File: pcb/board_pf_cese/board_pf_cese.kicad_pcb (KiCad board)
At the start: 2 copper layers, 120 x 100 mm, 17 parts, among them J1 Screw_Terminal_01x02, J2 Conn_01x04, J3 Conn_01x04, J4 Conn_01x04, J5 Conn_01x04, J6 Conn_01x15, J7 Conn_01x15, J8 Conn_01x08, J9 Conn_01x08

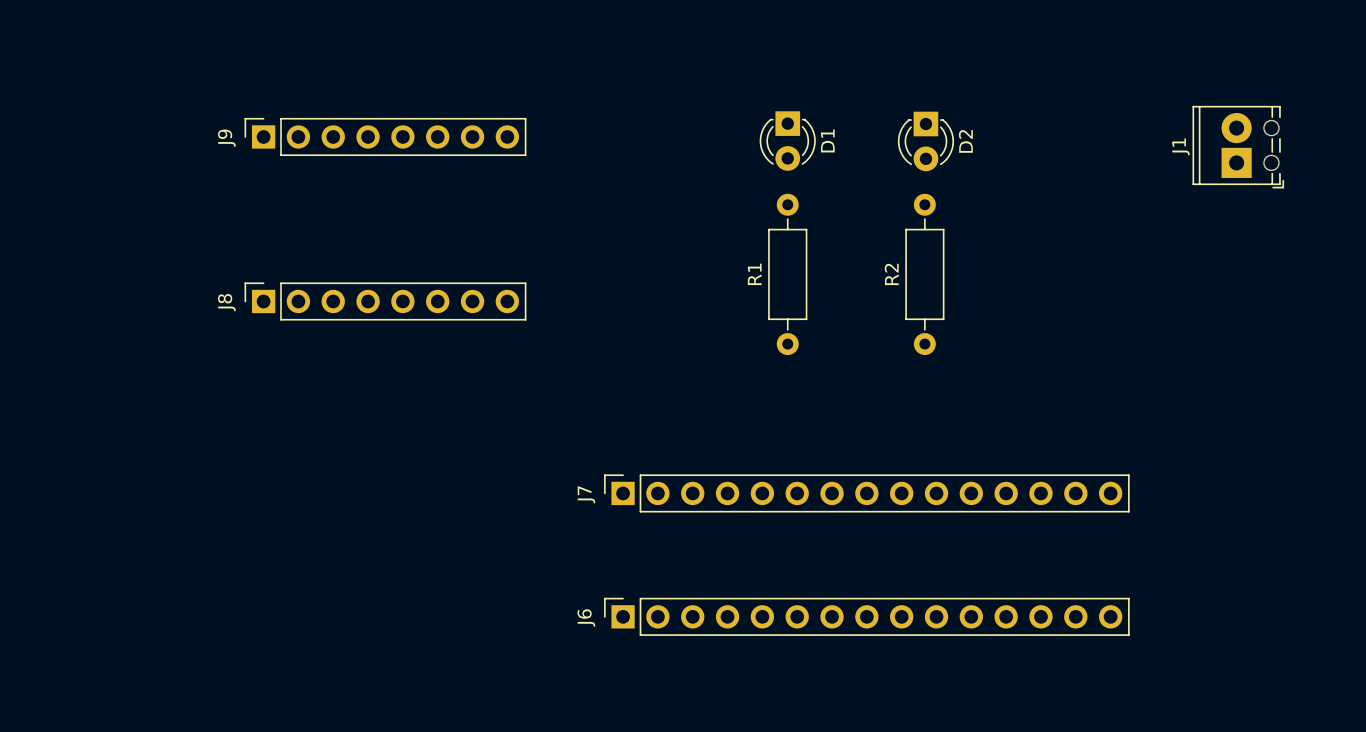
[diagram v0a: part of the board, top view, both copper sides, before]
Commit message: se agrego el archvo git ignore
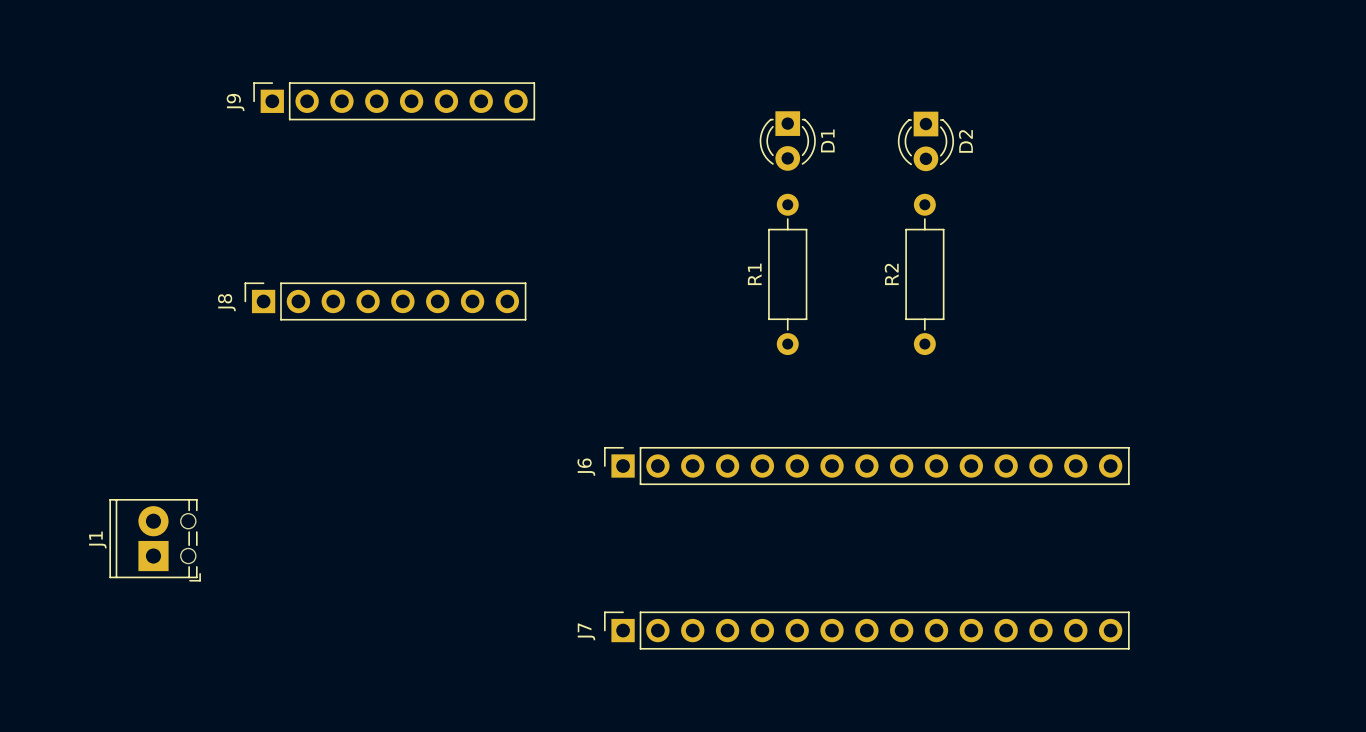
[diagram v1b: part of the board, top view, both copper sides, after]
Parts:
- moved J1 84.0 mm to (112.0, 107.5)
- moved J6 11.0 mm to (146.2, 101.0)
- moved J7 10.0 mm to (146.2, 113.0)
- moved J9 2.68 mm to (120.7, 74.4)
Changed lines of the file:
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@@
   )
   (footprint "TerminalBlock_Phoenix:TerminalBlock_Phoenix_MPT-0,5-2-2.54_1x02_P2.54mm_Horizontal" (layer "F.Cu")
-    (at 191 78.866 90)
+    (at 112 107.54 90)
     (descr "Terminal Block Phoenix MPT-0,5-2-2.54, 2 pins, pitch 2.54mm, size 5.54x6.2mm^2, drill diamater 1.1mm, pad diameter 2.2mm, see http://www.mouser.com/ds/2/324/ItemDetail_1725656-920552.pdf, script-generated using https://github.com/pointhi/kicad-footprint-generator/scripts/TerminalBlock_Phoenix")
     (tags "THT Terminal Block Phoenix MPT-0,5-2-2.54 pitch 2.54mm size 5.54x6.2mm^2 drill 1.1mm pad 2.2mm")
@@
   )
   (footprint "Connector_PinSocket_2.54mm:PinSocket_1x15_P2.54mm_Vertical" (layer "F.Cu")
-    (at 146.25 102.975 90)
+    (at 146.25 112.975 90)
     (descr "Through hole straight socket strip, 1x15, 2.54mm pitch, single row (from Kicad 4.0.7), script generated")
     (tags "Through hole socket strip THT 1x15 2.54mm single row")
@@
   )
   (footprint "Connector_PinSocket_2.54mm:PinSocket_1x08_P2.54mm_Vertical" (layer "F.Cu")
-    (at 120.03 76.975 90)
+    (at 120.665 74.375 90)
     (descr "Through hole straight socket strip, 1x08, 2.54mm pitch, single row (from Kicad 4.0.7), script generated")
     (tags "Through hole socket strip THT 1x08 2.54mm single row")
@@
   )
   (footprint "Connector_PinSocket_2.54mm:PinSocket_1x15_P2.54mm_Vertical" (layer "F.Cu")
-    (at 146.25 111.975 90)
+    (at 146.25 100.975 90)
     (descr "Through hole straight socket strip, 1x15, 2.54mm pitch, single row (from Kicad 4.0.7), script generated")
     (tags "Through hole socket strip THT 1x15 2.54mm single row")

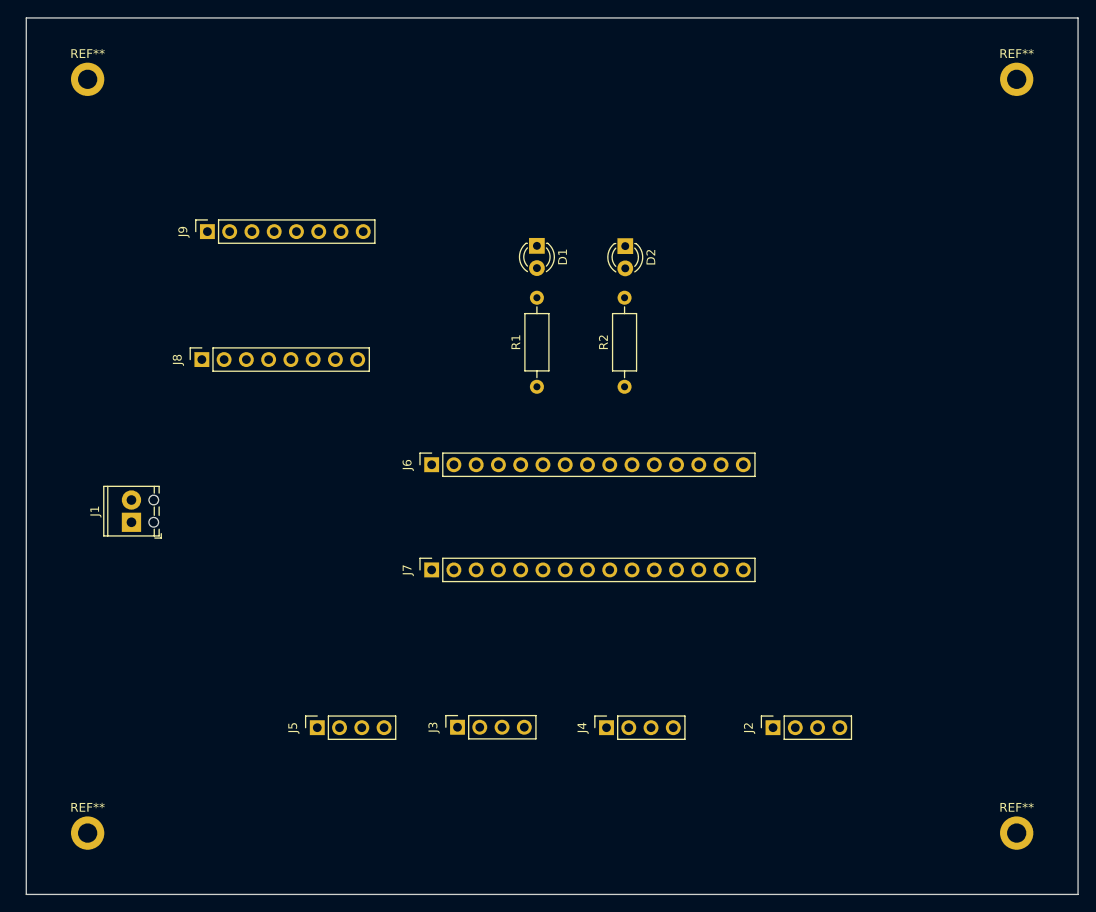
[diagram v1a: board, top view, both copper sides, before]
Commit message: se redimensiono el tamaño del pcb
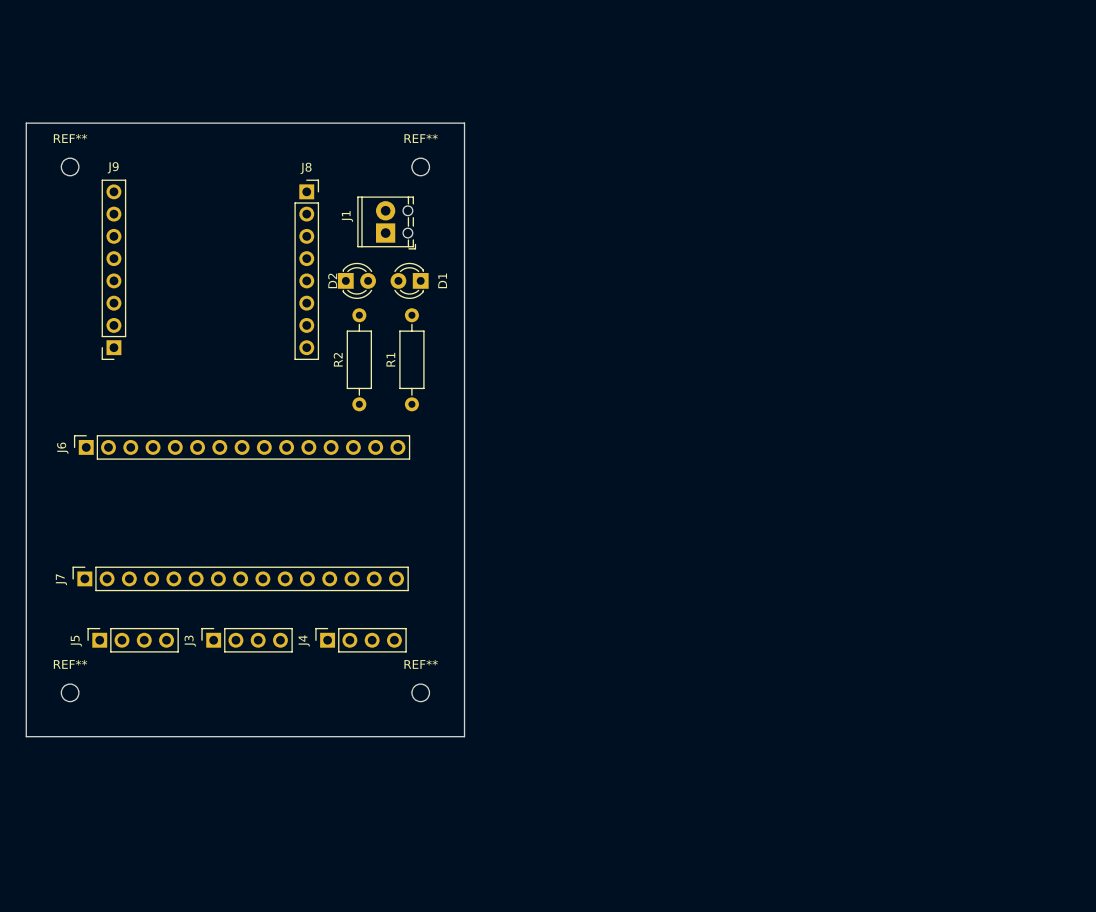
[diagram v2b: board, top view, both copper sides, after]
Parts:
- removed J2: Conn_01x04, Connector_PinSocket_2.54mm:PinSocket_1x04_P2.54mm_Vertical
- removed the REF** at (213.0, 143.0)
- removed the REF** at (107.0, 57.0)
- removed the REF** at (213.0, 57.0)
- removed the REF** at (107.0, 143.0)
- added REF**: MountingHole_2mm, MountingHole:MountingHole_2mm, F.Cu at (105.0, 127.0)
- added REF**: MountingHole_2mm, MountingHole:MountingHole_2mm, F.Cu at (105.0, 67.0)
- added REF**: MountingHole_2mm, MountingHole:MountingHole_2mm, F.Cu at (145.0, 127.0)
- added REF**: MountingHole_2mm, MountingHole:MountingHole_2mm, F.Cu at (145.0, 67.0)
- moved J1 43.9 mm to (141.0, 74.5)
- moved J7 39.6 mm to (106.7, 114.0)
- moved J6 39.5 mm to (106.8, 99.0)
- moved J4 33.3 mm to (134.4, 121.0)
- moved D2 32.1 mm to (136.5, 80.0), turned to 0 degrees
- moved R2 30.3 mm to (138.0, 94.1)
- moved J3 29.5 mm to (121.4, 121.0)
- moved J5 26.7 mm to (108.4, 121.0)
- moved J8 22.6 mm to (132.0, 69.8), turned to 0 degrees
- moved J9 17.0 mm to (110.0, 87.6), turned to 180 degrees
- moved R1 14.4 mm to (144.0, 94.1)
- moved D1 13.9 mm to (145.0, 80.0), turned to 180 degrees
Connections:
- J6 pad 6: Net-(J2-Pad4) -> unconnected-(J6-Pin_6-Pad6)
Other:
- board size 120 x 100 mm -> 50 x 70 mm

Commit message: ruteo con errores
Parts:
- added J2: Conn_01x04, Connector_PinSocket_2.54mm:PinSocket_1x04_P2.54mm_Vertical, F.Cu at (114.0, 122.0)
- moved J6 39.6 mm to (142.6, 116.0), turned to -90 degrees
- moved J7 38.2 mm to (142.6, 100.8), turned to -90 degrees
- moved J9 27.5 mm to (131.9, 71.0), turned to 0 degrees
- moved J8 23.0 mm to (109.0, 71.0)
- moved J5 21.5 mm to (129.0, 127.0)
- moved J4 21.2 mm to (114.0, 127.0)
- moved J3 7.61 mm to (128.9, 122.0)
- moved J1 3.00 mm to (144.0, 74.5)
- moved D2 2.73 mm to (139.0, 79.0), turned to -90 degrees
- moved R1 1.41 mm to (145.0, 95.1)
- moved R2 1.41 mm to (139.0, 95.1)
- moved D1 1.00 mm to (145.0, 79.0), turned to -90 degrees
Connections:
- J6 pad 10: unconnected-(J6-Pin_10-Pad10) -> Net-(J4-Pin_3)
- J6 pad 3: /N_RST -> unconnected-(J6-Pin_3-Pad3)
- J6 pad 4: +5V -> unconnected-(J6-Pin_4-Pad4)
- J6 pad 6: unconnected-(J6-Pin_6-Pad6) -> /SCL
- J6 pad 7: Net-(J3-Pin_4) -> unconnected-(J6-Pin_7-Pad7)
- J6 pad 8: Net-(J4-Pin_3) -> Net-(J3-Pin_4)
- J6 pad 9: unconnected-(J6-Pin_9-Pad9) -> Net-(J2-Pin_4)
- J7 pad 1: /SCL -> /M_TX
- J7 pad 10: Net-(J7-Pin_10) -> unconnected-(J7-Pin_10-Pad10)
- J7 pad 13: unconnected-(J7-Pin_13-Pad13) -> /SE
- J7 pad 15: unconnected-(J7-Pin_15-Pad15) -> /SDA
- J7 pad 2: /SDA -> /M_RX
- J7 pad 3: /N_RST -> unconnected-(J7-Pin_3-Pad3)
- J7 pad 5: unconnected-(J7-Pin_5-Pad5) -> /OR
- J7 pad 6: unconnected-(J7-Pin_6-Pad6) -> /SO
- J7 pad 7: /M_TX -> unconnected-(J7-Pin_7-Pad7)
- J7 pad 8: /M_RX -> unconnected-(J7-Pin_8-Pad8)
- J7 pad 9: /PU -> unconnected-(J7-Pin_9-Pad9)
- J8 pad 2: /PU -> /OR
- J9 pad 7: +5V -> unconnected-(J9-Pin_7-Pad7)
- R1 pad 1: Net-(J7-Pin_10) -> /SO
- R2 pad 1: +3.3V -> /SE
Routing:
- net /SDA: track 0.00 -> 67.8 mm
- net /OR: track 0.00 -> 47.6 mm
- net /SCL: track 0.00 -> 41.3 mm
- net /M_TX: track 0.00 -> 33.9 mm
- net /M_RX: track 0.00 -> 33.5 mm
- net /SE: track 0.00 -> 30.0 mm
- net Net-(J4-Pin_3): track 0.00 -> 27.8 mm
- net /SO: track 0.00 -> 19.3 mm
- net Net-(J3-Pin_4): track 0.00 -> 16.0 mm
- net Net-(J2-Pin_4): track 0.00 -> 6.26 mm
- net Net-(D2-A): track 0.00 -> 3.38 mm
- net Net-(D1-A): track 0.00 -> 3.38 mm
- added copper zone on F.Cu, net +3.3V
- added copper zone on B.Cu, net GND

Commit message: ruteo terminado
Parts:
- added REF**: KiCad-Logo2_5mm_SilkScreen, Symbol:KiCad-Logo2_5mm_SilkScreen, B.Cu at (124.0, 107.0)
- renumbered REF** to REF1, REF** to REF2, REF** to REF3, REF** to REF4
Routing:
- net GND: track 0.00 -> 8.71 mm, vias 0 -> 1
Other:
- board text added: "Ing. Mario Aguilar"

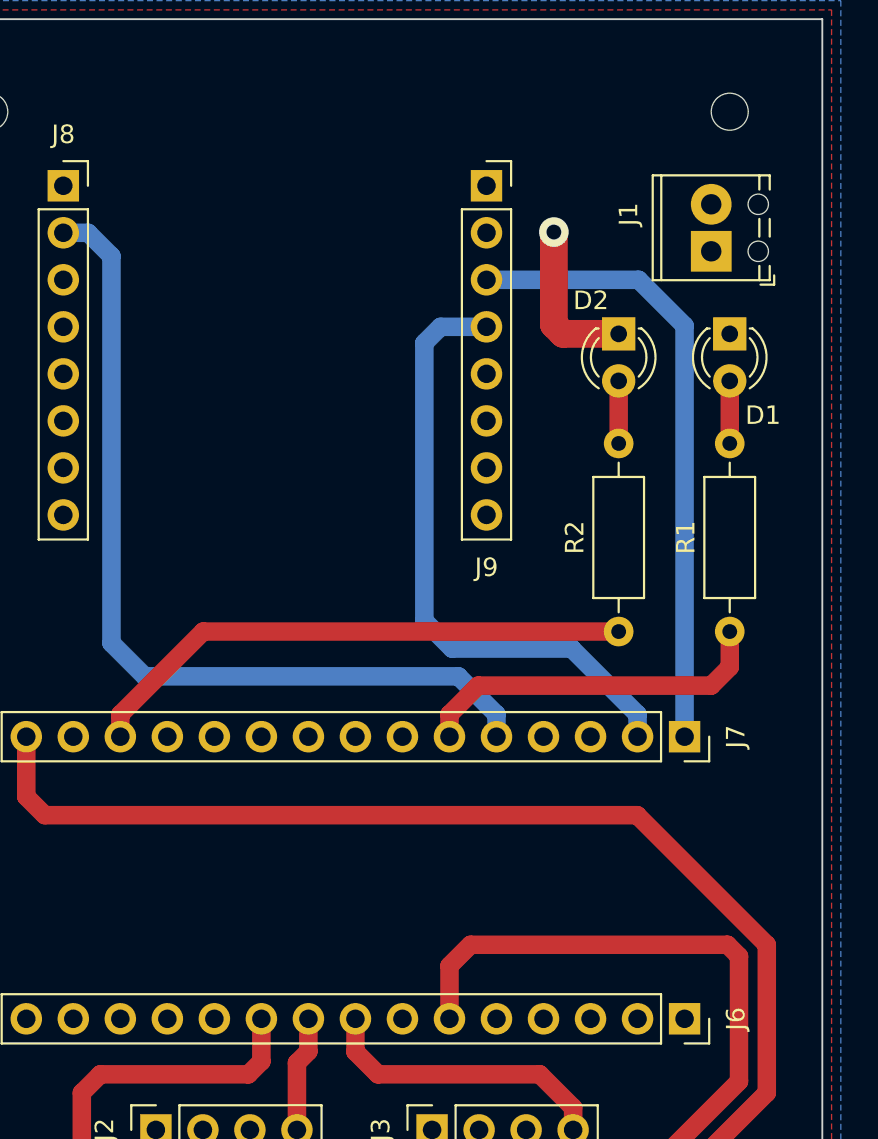
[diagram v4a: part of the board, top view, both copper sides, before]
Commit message: se actualizo el metodo de alimentacion
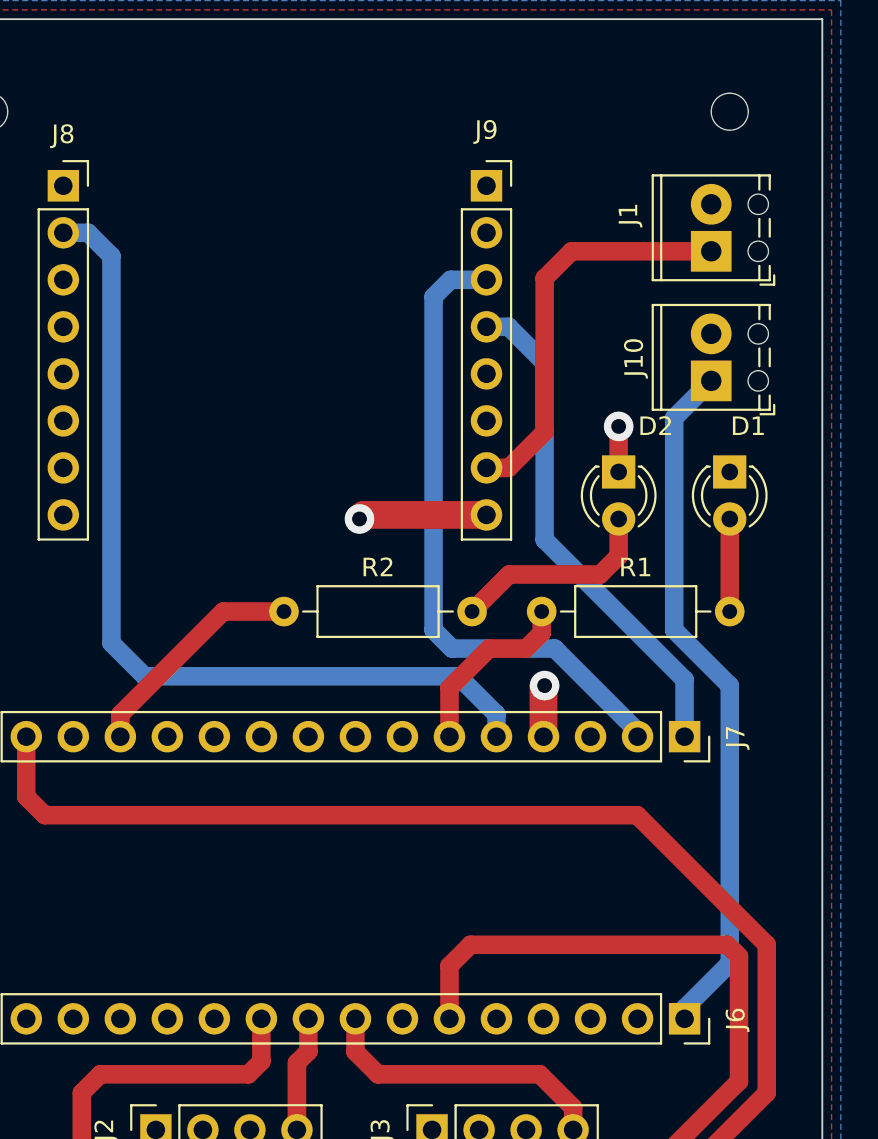
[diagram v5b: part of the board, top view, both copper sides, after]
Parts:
- added J10: Screw_Terminal_01x02, TerminalBlock_Phoenix:TerminalBlock_Phoenix_MPT-0,5-2-2.54_1x02_P2.54mm_Horizontal, F.Cu at (144.0, 81.5)
- moved R2 18.1 mm to (120.9, 94.0), turned to 0 degrees
- moved R1 10.2 mm to (134.8, 94.0), turned to 0 degrees
- moved D1 7.46 mm to (145.0, 86.5)
- moved D2 7.46 mm to (139.0, 86.5)
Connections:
- J1 pad 1: +3.3V -> +5V
- J6 pad 1: unconnected-(J6-Pin_1-Pad1) -> +12V
- J7 pad 1: /M_TX -> /M_RX
- J7 pad 2: /M_RX -> /M_TX
- J9 pad 7: unconnected-(J9-Pin_7-Pad7) -> +5V
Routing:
- net +12V: track 0.00 -> 37.5 mm
- net +5V: track 0.00 -> 21.8 mm
- net /SE: track 30.0 -> 12.3 mm
- net /SO: track 19.3 -> 9.99 mm
- net Net-(D2-A): track 3.38 -> 11.2 mm
- net /M_RX: track 33.5 -> 27.3 mm
- net GND: track 8.71 -> 12.2 mm, vias 1 -> 3
- net Net-(D1-A): track 3.38 -> 5.00 mm
- net /M_TX: track 33.9 -> 34.8 mm

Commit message: se adiciono conn uart2 para debug
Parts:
- added J11: Conn_01x05, Connector_PinSocket_2.54mm:PinSocket_1x05_P2.54mm_Vertical, F.Cu at (106.9, 96.0)
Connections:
- J6 pad 5: unconnected-(J6-Pin_5-Pad5) -> /UART2_TX
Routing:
- net /UART2_TX: track 0.00 -> 67.3 mm, vias 0 -> 1
- net /OR: track 47.6 -> 43.5 mm
- net /SCL: track 41.3 -> 42.9 mm
- net /SE: track 12.3 -> 13.6 mm

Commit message: corrigio posicionamiento del conn debug
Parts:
- moved J11 1.00 mm to (106.9, 95.0)
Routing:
- net /UART2_TX: track 67.3 -> 68.3 mm
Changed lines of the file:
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@@
   )
   (footprint "Connector_PinSocket_2.54mm:PinSocket_1x05_P2.54mm_Vertical" (layer "F.Cu")
-    (at 106.92 96 90)
+    (at 106.92 95 90)
     (descr "Through hole straight socket strip, 1x05, 2.54mm pitch, single row (from Kicad 4.0.7), script generated")
     (tags "Through hole socket strip THT 1x05 2.54mm single row")
@@
   (segment (start 107 107) (end 104 104) (width 1) (layer "F.Cu") (net 12))
   (segment (start 140 108) (end 139 107) (width 1) (layer "F.Cu") (net 12))
+  (segment (start 112 97.202081) (end 112 95) (width 1) (layer "F.Cu") (net 12))
   (segment (start 139 107) (end 107 107) (width 1) (layer "F.Cu") (net 12))
   (segment (start 111.202081 98) (end 112 97.202081) (width 1) (layer "F.Cu") (net 12))
@@
   (segment (start 105 98) (end 111.202081 98) (width 1) (layer "F.Cu") (net 12))
   (segment (start 104 104) (end 104 99) (width 1) (layer "F.Cu") (net 12))
-  (segment (start 112 97.202081) (end 112 96) (width 1) (layer "F.Cu") (net 12))
   (via (at 140 108) (size 1.6) (drill 0.8) (layers "F.Cu" "B.Cu") (net 12))
   (segment (start 139 114) (end 133 114) (width 1) (layer "B.Cu") (net 12))
